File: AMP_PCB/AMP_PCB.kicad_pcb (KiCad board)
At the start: 2 copper layers, 25 x 25 mm, 6 parts, among them J1 Conn_Coaxial, J2 Conn_Coaxial, J3 Conn_Coaxial, J4 Conn_Coaxial, J5 Conn_01x02_Pin

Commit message: updated footprint ver
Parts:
- added C1: 1n, Capacitor_SMD:C_1206_3216Metric, F.Cu at (180.9, 101.7)
- added C2: 1n, Capacitor_SMD:C_1206_3216Metric, F.Cu at (180.9, 105.0)
- added C3: 1.5m, Capacitor_SMD:C_1206_3216Metric, F.Cu at (180.9, 108.4)
- added C4: 1.5m, Capacitor_SMD:C_1206_3216Metric, F.Cu at (180.9, 111.7)
- added J3: Conn_Coaxial, Connector_Coaxial:SMA_Samtec_SMA-J-P-H-ST-EM1_EdgeMount, F.Cu at (165.4, 104.5)
- added J4: Conn_Coaxial, Connector_Coaxial:SMA_Samtec_SMA-J-P-H-ST-EM1_EdgeMount, F.Cu at (165.4, 113.6)
- added MOS2: JFE150DCKR, sim_foot:TRANS_JFE150DCKR, F.Cu at (169.6, 123.4)
- added R1: 200, Resistor_SMD:R_1206_3216Metric, F.Cu at (159.3, 101.7)
- added R2: 200, Resistor_SMD:R_1206_3216Metric, F.Cu at (159.3, 105.0)
- added R3: 5, Resistor_SMD:R_1206_3216Metric, F.Cu at (159.3, 108.3)
- added R4: 5, Resistor_SMD:R_1206_3216Metric, F.Cu at (159.3, 111.6)
- added R5: 80, Resistor_SMD:R_1206_3216Metric, F.Cu at (159.3, 114.9)
- added R6: 80, Resistor_SMD:R_1206_3216Metric, F.Cu at (159.3, 118.2)
- added R7: 1, Resistor_SMD:R_1206_3216Metric, F.Cu at (159.3, 121.5)
- added R8: 1, Resistor_SMD:R_1206_3216Metric, F.Cu at (159.3, 124.8)
- moved MOS1 61.2 mm to (169.6, 119.9)
- moved J5 49.5 mm to (164.4, 120.4)
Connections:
- J1 pad 1: unconnected-(J1-In-Pad1) -> GND
- J1 pad 2: unconnected-(J1-Ext-Pad2) -> Vgate1
- J2 pad 1: unconnected-(J2-In-Pad1) -> GND
- J2 pad 2: unconnected-(J2-Ext-Pad2) -> Vgate2
- J5 pad 1: Vgate -> GND
- J5 pad 2: Vdrain -> Vdd
- MOS1 pad 3: Vgate -> Net-(MOS1-G)
- MOS1 pad 5: Vdrain -> /Vout1
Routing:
- added copper zone on B.Cu, net (none)
- removed copper zone on B.Cu, net Vdrain

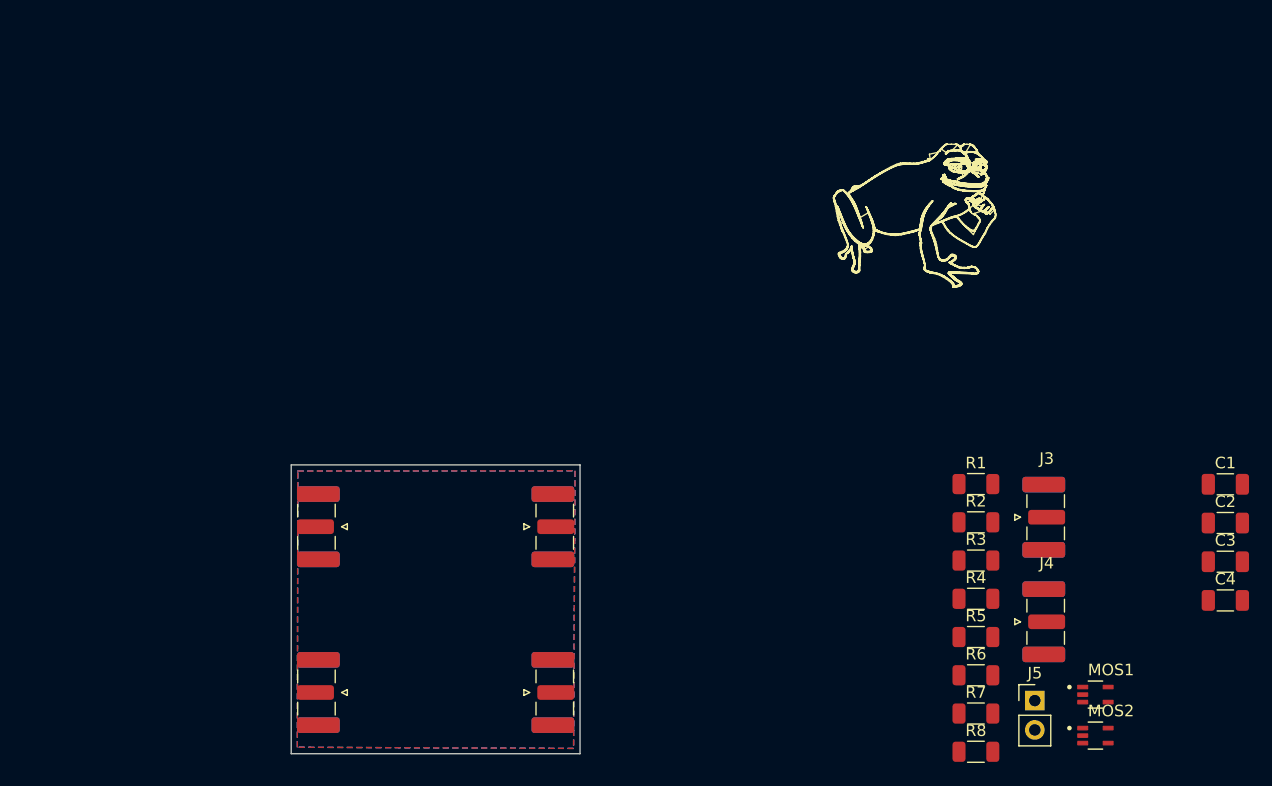
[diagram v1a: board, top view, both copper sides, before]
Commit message: updated design + footprints
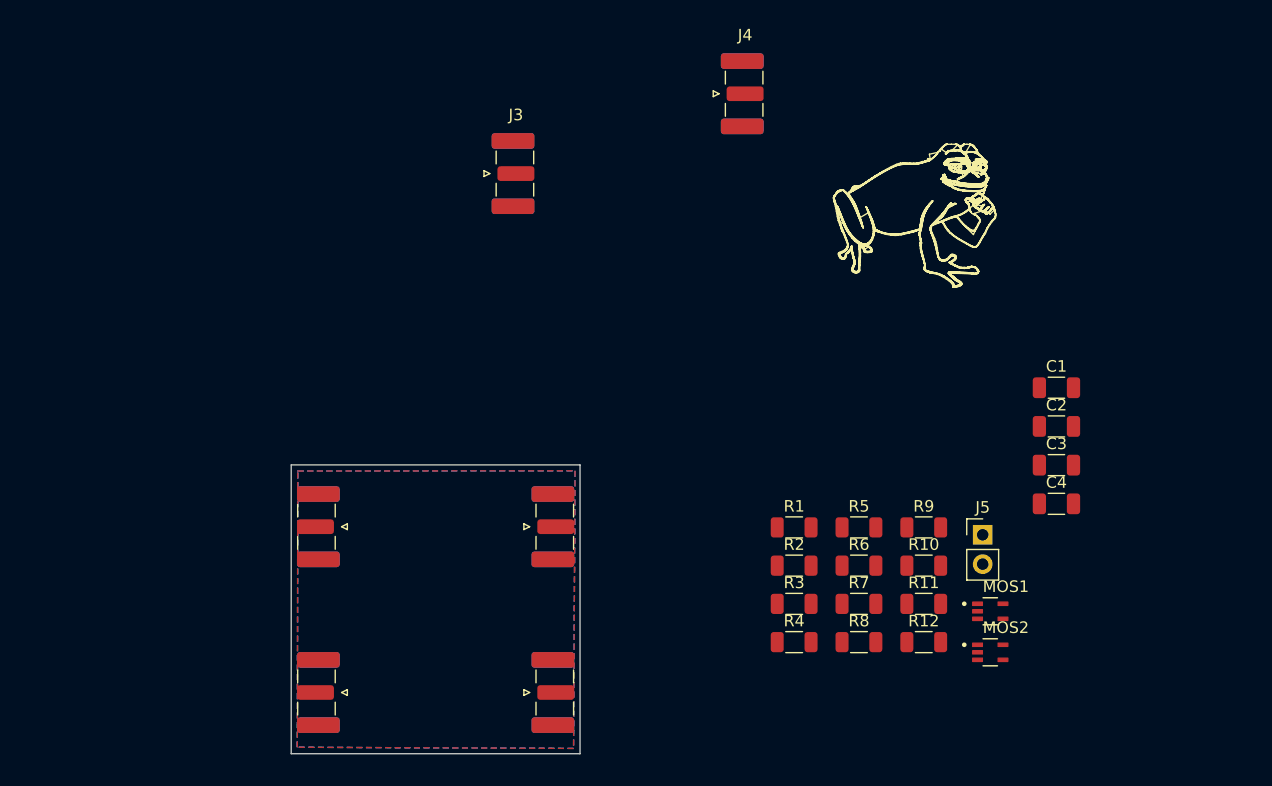
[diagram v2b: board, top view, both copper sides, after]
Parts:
- added R10: 180Ω, Resistor_SMD:R_1206_3216Metric, F.Cu at (154.8, 108.7)
- added R11: 500Ω, Resistor_SMD:R_1206_3216Metric, F.Cu at (154.8, 112.0)
- added R12: 500Ω, Resistor_SMD:R_1206_3216Metric, F.Cu at (154.8, 115.3)
- added R9: 180Ω, Resistor_SMD:R_1206_3216Metric, F.Cu at (154.8, 105.4)
- C1, C2: value 1n -> 1nF
- C3, C4: value 1.5m -> 100uF
- R1, R2: value 200 -> 15Ω
- R3, R4: value 5 -> 10Ω
- R5, R6: value 80 -> 300Ω
- R7, R8: value 1 -> 10Ω
- moved J3 54.7 mm to (119.5, 74.8)
- moved J4 52.6 mm to (139.3, 67.9)
- moved C1 16.8 mm to (166.2, 93.3)
- moved C2 16.8 mm to (166.2, 96.7)
- moved C3 16.8 mm to (166.2, 100.0)
- moved C4 16.8 mm to (166.2, 103.4)
- moved R1 16.2 mm to (143.5, 105.4)
- moved R2 16.2 mm to (143.5, 108.7)
- moved R3 16.2 mm to (143.5, 112.0)
- moved R4 16.2 mm to (143.5, 115.3)
- moved J5 15.0 mm to (159.9, 106.0)
- moved R5 13.9 mm to (149.1, 105.4)
- moved R6 13.9 mm to (149.1, 108.7)
- moved R7 13.9 mm to (149.1, 112.0)
- moved R8 13.9 mm to (149.1, 115.3)
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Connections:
- R1 pad 1: Vdd -> Net-(R1-Pad1)
- R2 pad 1: Vdd -> Net-(R10-Pad2)
- R5 pad 1: Vdd -> Net-(R11-Pad2)
- R6 pad 1: Vdd -> Net-(R12-Pad2)

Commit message: traces and pcb
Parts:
- removed the J3 at (122.9, 105.3)
- removed the J4 at (122.9, 119.7)
- moved C4 59.4 mm to (110.3, 123.4)
- moved J5 57.7 mm to (102.5, 112.2), turned to 90 degrees
- moved C1 54.8 mm to (112.2, 102.4)
- moved J4 54.4 mm to (122.9, 119.7)
- moved C3 54.4 mm to (112.2, 105.4), turned to 180 degrees
- moved C2 52.6 mm to (119.0, 119.8), turned to 90 degrees
- moved R9 46.3 mm to (108.6, 109.2), turned to 90 degrees
- moved R12 46.1 mm to (108.7, 116.5), turned to -90 degrees
- moved MOS2 45.1 mm to (115.7, 120.8)
- moved MOS1 44.5 mm to (117.2, 102.5)
- moved R11 41.5 mm to (113.3, 112.0), turned to 90 degrees
- moved R6 40.7 mm to (110.3, 120.9)
- moved R10 38.0 mm to (117.0, 113.2)
- moved R8 34.9 mm to (115.2, 123.4)
- moved R7 32.8 mm to (117.0, 105.4)
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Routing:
- net GND: track 0.00 -> 37.8 mm
- net /Vout1: track 0.00 -> 20.7 mm
- net Vdd: track 0.00 -> 15.7 mm
- net Vgate1: track 0.00 -> 15.6 mm
- net /Vout2: track 0.00 -> 14.7 mm
- net Vgate2: track 0.00 -> 12.5 mm
- net Net-(MOS1-G): track 0.00 -> 11.5 mm
- net Net-(MOS2-G): track 0.00 -> 6.70 mm
- net Net-(R10-Pad2): track 0.00 -> 3.25 mm
- net Net-(R12-Pad2): track 0.00 -> 3.04 mm
- net Net-(R2-Pad2): track 0.00 -> 2.52 mm
- net Net-(R11-Pad2): track 0.00 -> 2.32 mm
- net Net-(R1-Pad1): track 0.00 -> 2.27 mm
- net Net-(R1-Pad2): track 0.00 -> 1.95 mm
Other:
- board text added: "Malithi was here"
- board text added: "Phoebe was here"

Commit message: etc
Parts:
- moved R8 37.1 mm to (79.7, 112.6), turned to 90 degrees
- moved R6 31.8 mm to (81.3, 108.0)
- moved MOS2 27.3 mm to (89.7, 112.4), turned to -90 degrees
- moved R12 26.1 mm to (82.8, 112.7), turned to 90 degrees
- moved MOS1 20.3 mm to (134.0, 113.8), turned to 90 degrees
- moved C4 13.1 mm to (102.4, 113.0), turned to 90 degrees
- moved J5 11.6 mm to (113.8, 114.3), turned to -90 degrees
- moved R5 10.5 mm to (109.2, 103.6), turned to -90 degrees
- moved R10 9.19 mm to (112.9, 121.3), turned to -90 degrees
- moved R7 8.44 mm to (109.2, 108.8), turned to -90 degrees
- moved R11 8.42 mm to (112.4, 103.6)
- moved C1 7.95 mm to (118.8, 106.9), turned to -90 degrees
- moved C2 7.87 mm to (122.7, 112.9), turned to -90 degrees
- moved C3 6.10 mm to (106.3, 103.6), turned to 90 degrees
- moved R2 5.70 mm to (115.6, 121.4), turned to 90 degrees
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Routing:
- net GND: track 37.8 -> 1.67 mm
- net Vdd: track 15.7 -> 2.29 mm
- net /Vout1: track 20.7 -> 13.5 mm
- net Vgate2: track 12.5 -> 5.65 mm
- net Net-(MOS2-G): track 6.70 -> 0.00 mm
- net Net-(MOS1-G): track 11.5 -> 5.16 mm
- net Vgate1: track 15.6 -> 9.76 mm
- net /Vout2: track 14.7 -> 9.98 mm
- net Net-(R10-Pad2): track 3.25 -> 0.00 mm
- net Net-(R12-Pad2): track 3.04 -> 0.00 mm
- net Net-(R1-Pad1): track 2.27 -> 3.99 mm
- net (no net): track 0.00 -> 1.34 mm
- net Net-(R1-Pad2): track 1.95 -> 3.12 mm
- net Net-(R11-Pad2): track 2.32 -> 3.23 mm
- added copper zone on B.Cu, net Vdd
- removed copper zone on B.Cu, net (none)
- removed copper zone on B.Cu, net GND
